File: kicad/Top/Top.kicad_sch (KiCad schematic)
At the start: 2 parts

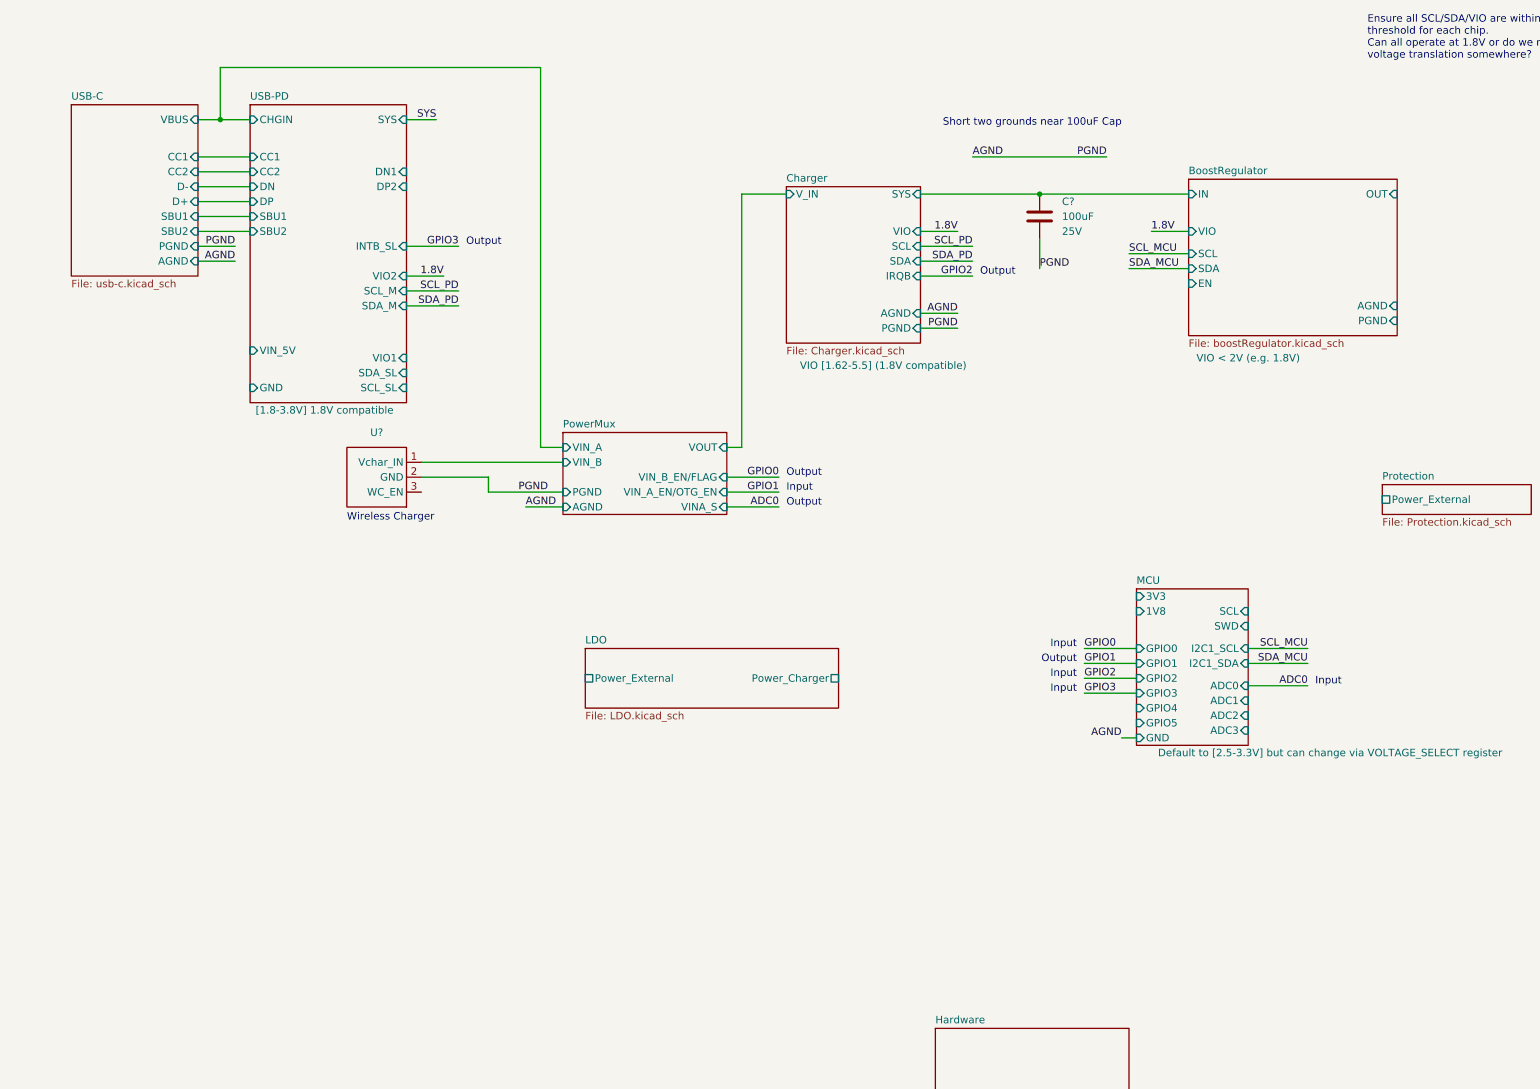
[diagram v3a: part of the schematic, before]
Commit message: Added switches for swapping I2C master between MCU and external
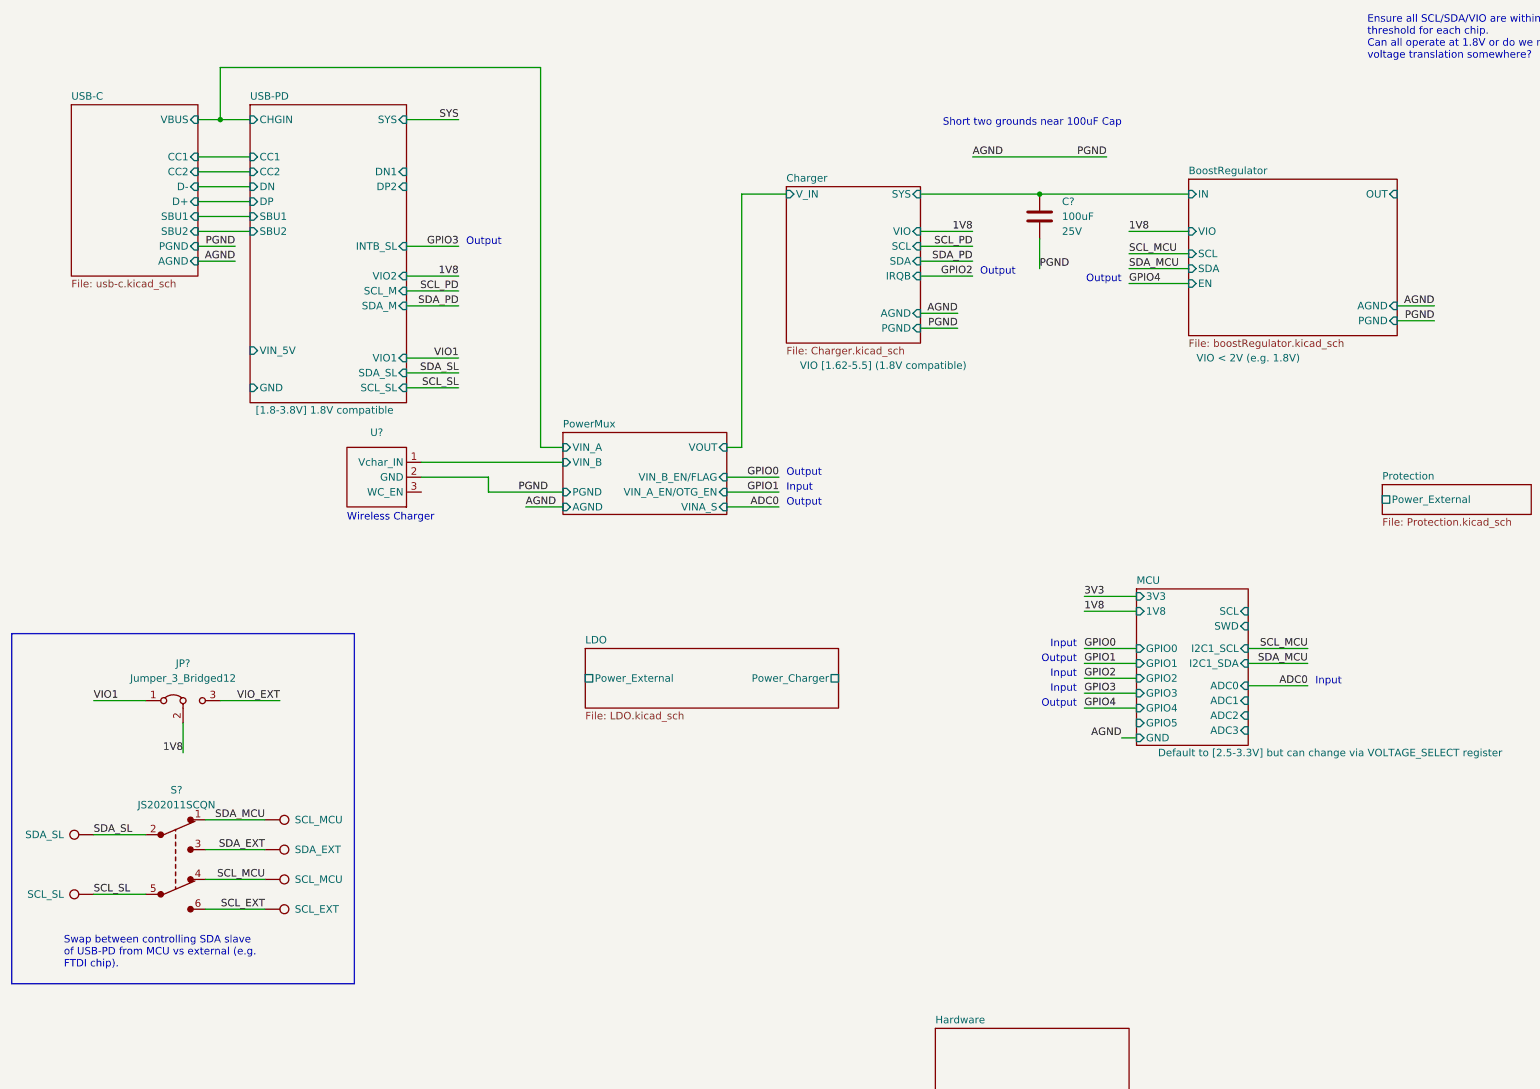
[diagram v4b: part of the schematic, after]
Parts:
- added JP?: Jumper_3_Bridged12, symbol Jumper:Jumper_3_Bridged12
- added S?: JS202011SCQN, digikey-footprints:Switch_Slide_JS202011SCQN, symbol dk_Slide-Switches:JS202011SCQN
- added TP?: SCL_SL, symbol Connector:TestPoint
- added TP? (x2): SCL_MCU, symbol Connector:TestPoint
- added TP?: SCL_EXT, symbol Connector:TestPoint
- added TP?: SDA_EXT, symbol Connector:TestPoint
- added TP?: SDA_SL, symbol Connector:TestPoint
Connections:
- net SCL_MCU: now also S?.4, TP?.1
- net SDA_MCU: now also S?.1, TP?.1
- new net 1V8: JP?.2 (C)
- new net SCL_EXT: S?.6, TP?.1
- new net SCL_SL: S?.5, TP?.1
- new net SDA_EXT: S?.3, TP?.1
- new net SDA_SL: S?.2, TP?.1
- new net VIO1: JP?.1 (A)
- new net VIO_EXT: JP?.3 (B)
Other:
- note added: "Swap between controlling SDA slave of USB-PD from MCU vs external (e.g. FTDI chip)."

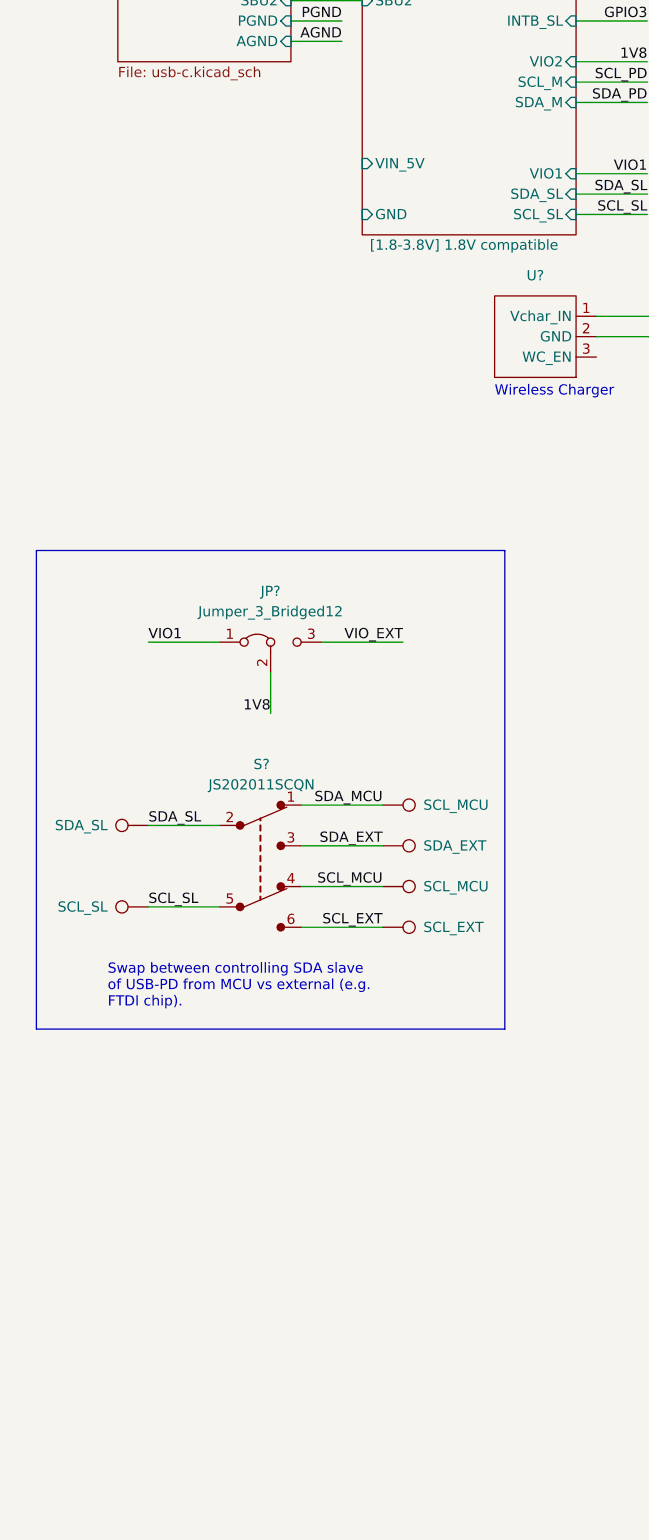
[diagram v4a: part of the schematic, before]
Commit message: Removed TP from PD GND terminals and connected to AGND
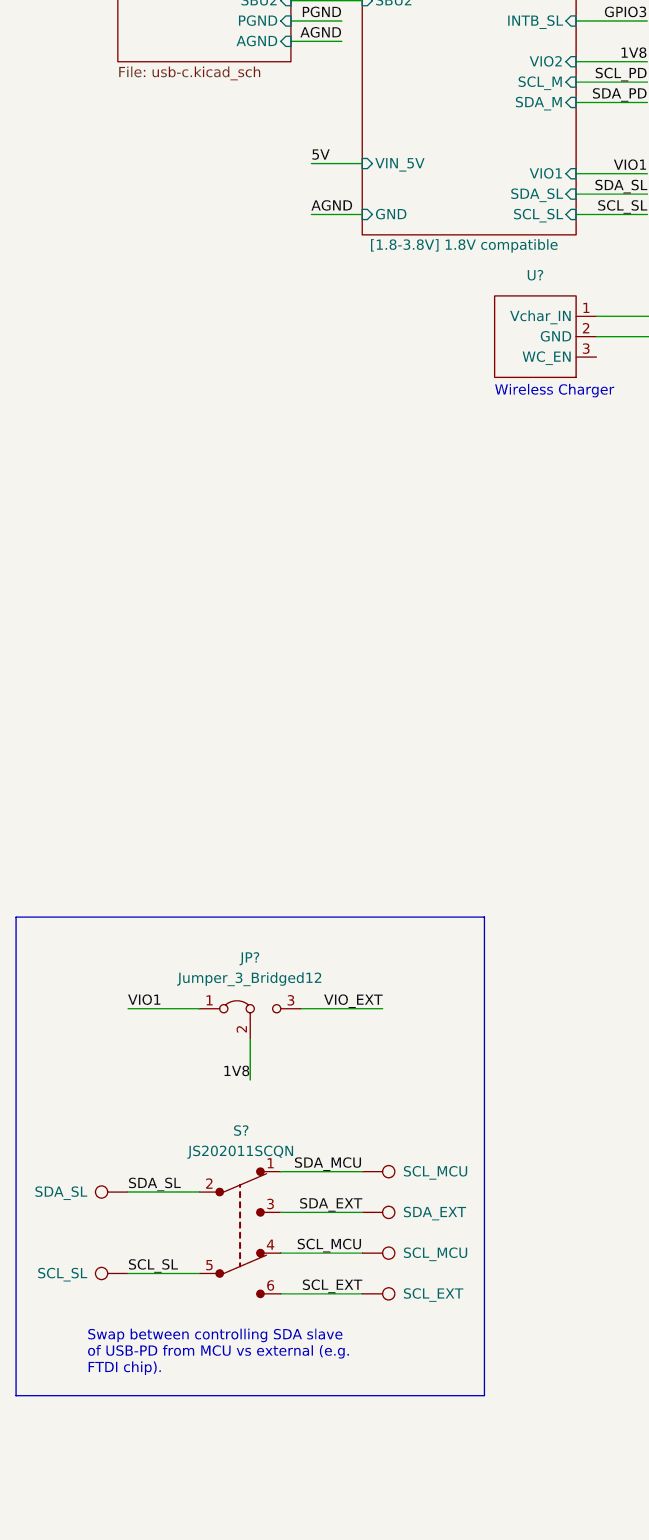
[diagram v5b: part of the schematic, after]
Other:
- moved on the sheet: JP?, S?

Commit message: wip
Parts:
- U?: EN_V (none) -> from min 1.4V - 28V
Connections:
- net BoostRegulator/IN is gone; now on net SYS: C?.1
- net GPIO5: now reaches U?.3 (WC_EN)
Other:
- sheet LDO renamed LDOs
- sheet LDOs ports: added none; removed Power_Charger, Power_External
- sheet USB-PD ports: added none; removed VIN_5V
- note added: "Wireless Charger Pull WC_EN low to enable"
- note removed: "Wireless Charger"
- moved on the sheet: U?
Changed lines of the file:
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@@
+    (stroke (width 0) (type default) (color 0 0 0 0))
+  )
+  (wire (pts (xy 66.04 85.09) (xy 57.15 85.09))
     (stroke (width 0) (type default) (color 0 0 0 0))
   )
@@
     (stroke (width 0) (type default) (color 0 0 0 0))
   )
+  (wire (pts (xy 241.3 34.29) (xy 252.73 34.29))
+    (stroke (width 0) (type default) (color 0 0 0 0))
+  )
   (wire (pts (xy 36.83 30.48) (xy 45.72 30.48))
     (stroke (width 0) (type default) (color 0 0 0 0))
@@
     (stroke (width 0) (type default) (color 0 0 0 0))
   )
+  (wire (pts (xy 130.81 124.46) (xy 121.92 124.46))
+    (stroke (width 0) (type default) (color 0 0 0 0))
+  )
   (wire (pts (xy 160.02 45.72) (xy 168.91 45.72))
     (stroke (width 0) (type default) (color 0 0 0 0))
@@
     (stroke (width 0) (type default) (color 0 0 0 0))
   )
+  (wire (pts (xy 187.96 124.46) (xy 196.85 124.46))
+    (stroke (width 0) (type default) (color 0 0 0 0))
+  )
   (wire (pts (xy 35.56 191.77) (xy 45.72 191.77))
     (stroke (width 0) (type default) (color 0 0 0 0))
@@
     (stroke (width 0) (type default) (color 0 0 0 0))
   )
-  (wire (pts (xy 86.36 85.09) (xy 99.06 85.09))
+  (wire (pts (xy 68.58 85.09) (xy 99.06 85.09))
     (stroke (width 0) (type default) (color 0 0 0 0))
   )
@@
     (stroke (width 0) (type default) (color 0 0 0 0))
   )
-  (wire (pts (xy 45.72 60.96) (xy 39.37 60.96))
+  (wire (pts (xy 102.87 116.84) (xy 93.98 116.84))
     (stroke (width 0) (type default) (color 0 0 0 0))
   )
@@
     (stroke (width 0) (type default) (color 0 0 0 0))
   )
+  (wire (pts (xy 130.81 118.11) (xy 121.92 118.11))
+    (stroke (width 0) (type default) (color 0 0 0 0))
+  )
   (wire (pts (xy 35.56 186.69) (xy 45.72 186.69))
     (stroke (width 0) (type default) (color 0 0 0 0))
@@
     (stroke (width 0) (type default) (color 0 0 0 0))
   )
-  (wire (pts (xy 74.93 80.01) (xy 99.06 80.01))
+  (wire (pts (xy 57.15 80.01) (xy 99.06 80.01))
     (stroke (width 0) (type default) (color 0 0 0 0))
   )
@@
     (stroke (width 0) (type default) (color 0 0 0 0))
   )
-  (wire (pts (xy 74.93 82.55) (xy 86.36 82.55))
+  (wire (pts (xy 57.15 82.55) (xy 68.58 82.55))
     (stroke (width 0) (type default) (color 0 0 0 0))
   )
@@
     (stroke (width 0) (type default) (color 0 0 0 0))
   )
-  (wire (pts (xy 86.36 82.55) (xy 86.36 85.09))
+  (wire (pts (xy 121.92 113.03) (xy 130.81 113.03))
+    (stroke (width 0) (type default) (color 0 0 0 0))
+  )
+  (wire (pts (xy 68.58 82.55) (xy 68.58 85.09))
     (stroke (width 0) (type default) (color 0 0 0 0))
   )
@@
     (stroke (width 0) (type default) (color 0 0 0 0))
   )
-  (text "Wireless Charger" (at 62.23 90.17 0)
+  (text "Wireless Charger\nPull WC_EN low to enable" (at 43.18 95.25 0)
     (effects (font (size 1.27 1.27)) (justify left bottom))
   )
@@
     (effects (font (size 1.27 1.27)) (justify right bottom))
   )
+  (text "Output" (at 186.69 124.46 180)
+    (effects (font (size 1.27 1.27)) (justify right bottom))
+  )
   (text "Swap between controlling SDA slave\nof USB-PD from MCU vs external (e.g.\nFTDI chip)."
     (at 11.43 212.09 0)
@@
     (effects (font (size 1.27 1.27)) (justify right bottom))
   )
+  (label "GPIO5" (at 66.04 85.09 180)
+    (effects (font (size 1.27 1.27)) (justify right bottom))
+  )
   (label "SCL_EXT" (at 45.72 201.93 180)
     (effects (font (size 1.27 1.27)) (justify right bottom))
@@
     (effects (font (size 1.27 1.27)) (justify left bottom))
   )
-  (label "5V" (at 39.37 60.96 0)
-    (effects (font (size 1.27 1.27)) (justify left bottom))
-  )
   (label "VIO_EXT" (at 48.26 166.37 180)
     (effects (font (size 1.27 1.27)) (justify right bottom))
@@
     (effects (font (size 1.27 1.27)) (justify left bottom))
   )
+  (label "SYS" (at 93.98 116.84 0)
+    (effects (font (size 1.27 1.27)) (justify left bottom))
+  )
   (label "SDA_PD" (at 168.91 45.72 180)
     (effects (font (size 1.27 1.27)) (justify right bottom))
@@
     (effects (font (size 1.27 1.27)) (justify right bottom))
   )
+  (label "1V8" (at 130.81 124.46 180)
+    (effects (font (size 1.27 1.27)) (justify right bottom))
+  )
   (label "SDA_EXT" (at 45.72 191.77 180)
     (effects (font (size 1.27 1.27)) (justify right bottom))
@@
     (effects (font (size 1.27 1.27)) (justify right bottom))
   )
+  (label "VBoost" (at 252.73 34.29 180)
+    (effects (font (size 1.27 1.27)) (justify right bottom))
+  )
   (label "SCL_SL" (at 16.51 199.39 0)
     (effects (font (size 1.27 1.27)) (justify left bottom))
@@
     (effects (font (size 1.27 1.27)) (justify left bottom))
   )
+  (label "GPIO5" (at 187.96 124.46 0)
+    (effects (font (size 1.27 1.27)) (justify left bottom))
+  )
   (label "GPIO3" (at 187.96 119.38 0)
     (effects (font (size 1.27 1.27)) (justify left bottom))
@@
     (effects (font (size 1.27 1.27)) (justify right bottom))
   )
+  (label "5V" (at 130.81 113.03 180)
+    (effects (font (size 1.27 1.27)) (justify right bottom))
+  )
   (label "GPIO0" (at 135.89 82.55 180)
     (effects (font (size 1.27 1.27)) (justify right bottom))
@@
     (effects (font (size 1.27 1.27)) (justify right bottom))
   )
+  (label "3V3" (at 130.81 118.11 180)
+    (effects (font (size 1.27 1.27)) (justify right bottom))
+  )
   (label "1V8" (at 195.58 40.64 0)
     (effects (font (size 1.27 1.27)) (justify left bottom))
@@
   )
   (label "SYS" (at 81.28 21.59 180)
+    (effects (font (size 1.27 1.27)) (justify right bottom))
+  )
+  (label "SYS" (at 180.34 34.29 180)
     (effects (font (size 1.27 1.27)) (justify right bottom))
   )
@@
     (pin "1")
   )
-  (symbol (lib_id "custom_modules:WRM483265-10F5-12V-G") (at 67.31 82.55 0) (unit 1)
-    (in_bom yes) (on_board yes) (fields_autoplaced)
-    (property "Reference" "U?" (id 0) (at 67.31 74.93 0))
-    (property "Value" "WRM483265-10F5-12V-G" (id 1) (at 67.31 74.93 0)
-      (effects (font (size 1.27 1.27)) hide)
-    )
-    (property "Footprint" "custom_modules:WRM483265-10F5-12V-G" (id 2) (at 67.31 74.93 0)
-      (effects (font (size 1.27 1.27)) hide)
-    )
-    (property "Datasheet" "" (id 3) (at 67.31 74.93 0)
-      (effects (font (size 1.27 1.27)) hide)
-    )
-    (property "Part Number" "WRM483265-10F5-12V-G" (id 4) (at 67.31 82.55 0)
-      (effects (font (size 1.27 1.27)) hide)
-    )
-    (property "Description" "Premade Wireless Rx Module (Seperate board, this represents just the connector pins)." (id 5) (at 67.31 82.55 0)
-      (effects (font (size 1.27 1.27)) hide)
-    )
+  (symbol (lib_id "custom_modules:WRM483265-10F5-12V-G") (at 49.53 82.55 0) (unit 1)
+    (in_bom yes) (on_board yes)
+    (property "Reference" "U?" (id 0) (at 49.53 74.93 0))
+    (property "Value" "WRM483265-10F5-12V-G" (id 1) (at 49.53 74.93 0)
+      (effects (font (size 1.27 1.27)) hide)
+    )
+    (property "Footprint" "custom_modules:WRM483265-10F5-12V-G" (id 2) (at 49.53 74.93 0)
+      (effects (font (size 1.27 1.27)) hide)
+    )
+    (property "Datasheet" "https://www.renesas.com/us/en/document/dst/p9221-r3-datasheet?language=en&r=394816" (id 3) (at 49.53 74.93 0)
+      (effects (font (size 1.27 1.27)) hide)
+    )
+    (property "Part Number" "WRM483265-10F5-12V-G" (id 4) (at 49.53 82.55 0)
+      (effects (font (size 1.27 1.27)) hide)
+    )
+    (property "Description" "Premade Wireless Rx Module (Seperate board, this represents just the connector pins)." (id 5) (at 49.53 82.55 0)
+      (effects (font (size 1.27 1.27)) hide)
+    )
+    (property "EN_V" "from min 1.4V - 28V" (id 13) (at 54.61 88.9 0))
     (pin "1")
     (pin "2")
@@
     (pin "2")
   )
-  (sheet (at 102.87 111.76) (size 43.18 10.16) (fields_autoplaced)
+  (sheet (at 102.87 111.76) (size 19.05 13.97) (fields_autoplaced)
     (stroke (width 0) (type solid) (color 128 0 0 1))
     (fill (color 0 0 0 0.0000))
-    (property "Sheet name" "LDO" (id 0) (at 102.87 111.0484 0)
+    (property "Sheet name" "LDOs" (id 0) (at 102.87 111.0484 0)
       (effects (font (size 1.27 1.27)) (justify left bottom))
     )
-    (property "Sheet file" "LDO.kicad_sch" (id 1) (at 102.87 122.5046 0)
+    (property "Sheet file" "LDO.kicad_sch" (id 1) (at 102.87 126.3146 0)
       (effects (font (size 1.27 1.27)) (justify left top))
-    )
-    (pin "Power_External" passive (at 102.87 116.84 180)
-      (effects (font (size 1.27 1.27)) (justify left))
-    )
-    (pin "Power_Charger" passive (at 146.05 116.84 0)
-      (effects (font (size 1.27 1.27)) (justify right))
     )
   )
@@
       (effects (font (size 1.27 1.27)) (justify left))
     )
-    (pin "VIN_5V" input (at 45.72 60.96 180)
-      (effects (font (size 1.27 1.27)) (justify left))
-    )
